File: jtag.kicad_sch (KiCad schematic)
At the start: 1 part, among them J3 PinHeader_2x7_P2mm_SMD_Shroud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

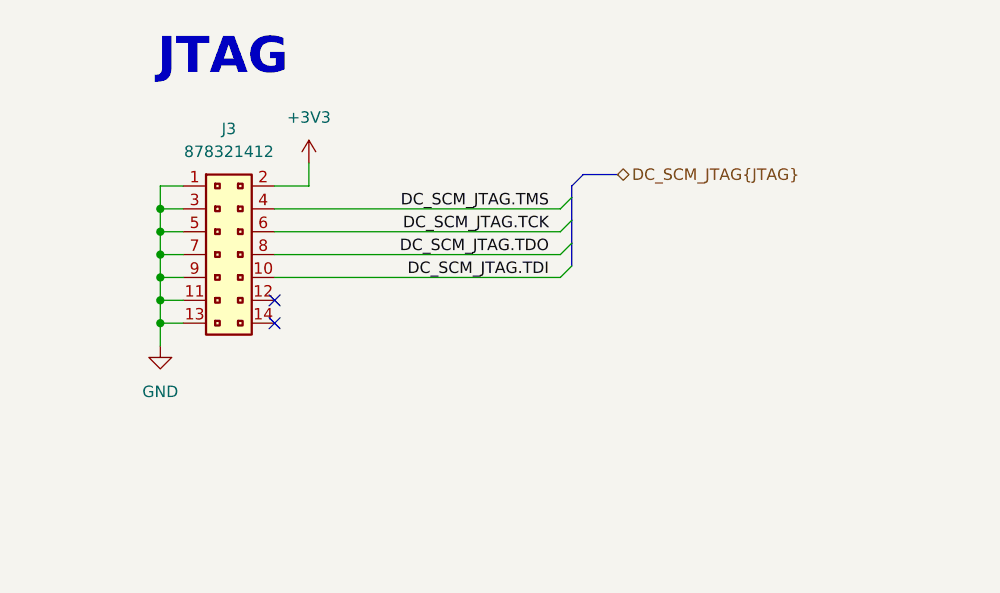
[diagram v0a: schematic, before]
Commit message: [#92504] Clear Wire BUS errors
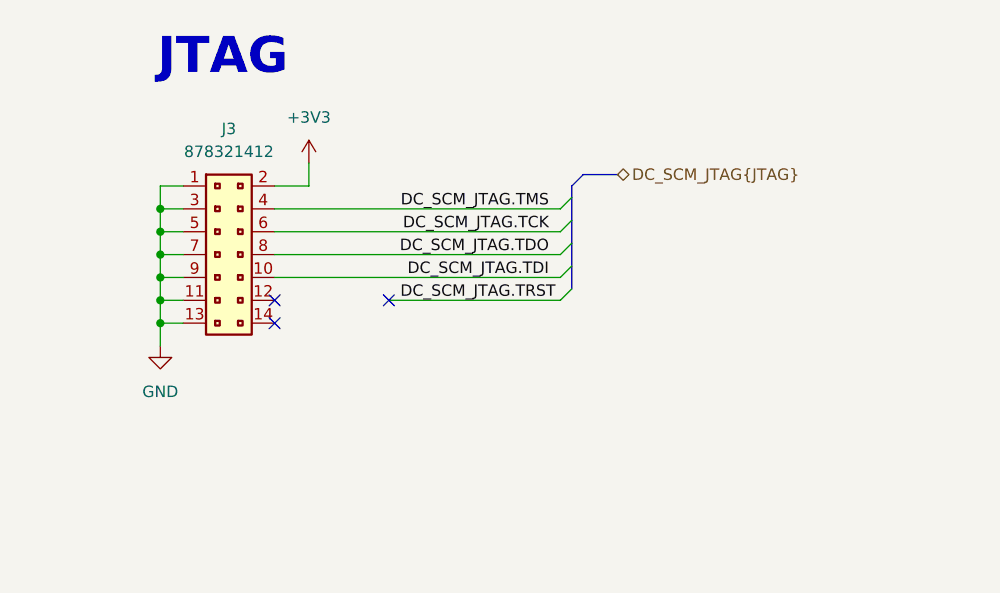
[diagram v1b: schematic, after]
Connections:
- no-connect marks 2 -> 3
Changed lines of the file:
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@@
+	)
+	(no_connect
+		(at 78.74 50.8)
 	)
 	(no_connect
@@
 	)
 	(bus_entry
+		(at 99.06 49.53)
+		(size -1.27 1.27)
+		(stroke
+			(width 0)
+			(type default)
+		)
+	)
+	(bus_entry
 		(at 99.06 41.91)
 		(size -1.27 1.27)
@@
 	(wire
 		(pts
+			(xy 78.74 50.8) (xy 97.79 50.8)
+		)
+		(stroke
+			(width 0)
+			(type default)
+		)
+	)
+	(wire
+		(pts
 			(xy 53.34 50.8) (xy 53.34 53.34)
 		)
@@
 		(pts
 			(xy 53.34 43.18) (xy 53.34 45.72)
+		)
+		(stroke
+			(width 0)
+			(type default)
+		)
+	)
+	(bus
+		(pts
+			(xy 99.06 46.99) (xy 99.06 49.53)
 		)
 		(stroke
@@
 		)
 	)
+	(label "DC_SCM_JTAG.TRST"
+		(at 80.01 50.8 0)
+		(effects
+			(font
+				(size 1.27 1.27)
+			)
+			(justify left bottom)
+		)
+	)

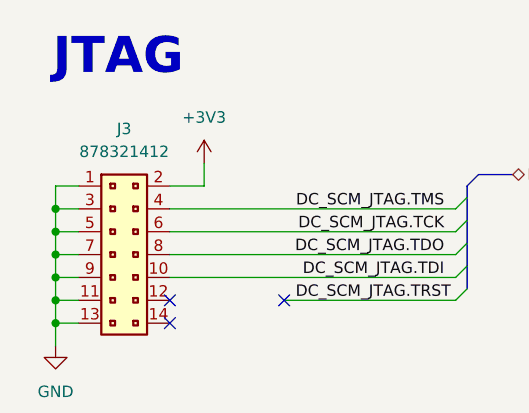
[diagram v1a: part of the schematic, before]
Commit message: [#92504] Update Annotation for connectors
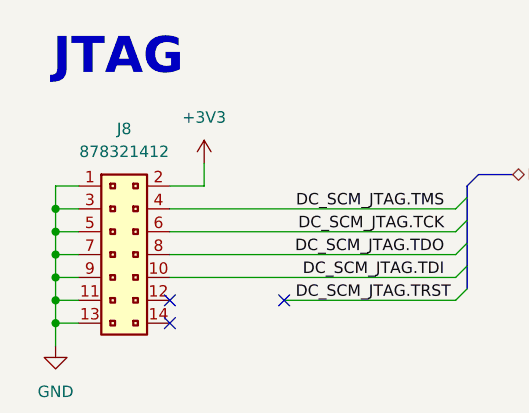
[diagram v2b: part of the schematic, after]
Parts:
- renumbered J3 to J8
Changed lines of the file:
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@@
 		(dnp no)
 		(fields_autoplaced yes)
-		(property "Reference" "J3"
+		(property "Reference" "J8"
 			(at 60.96 31.75 0)
 			(effects
@@
 			(project ""
 				(path "/5d67ef28-5805-4f87-b722-2926dabf7f6e/7d9b23ce-a430-4fe9-932d-039608fe4530"
-					(reference "J3")
+					(reference "J8")
 					(unit 1)
 				)

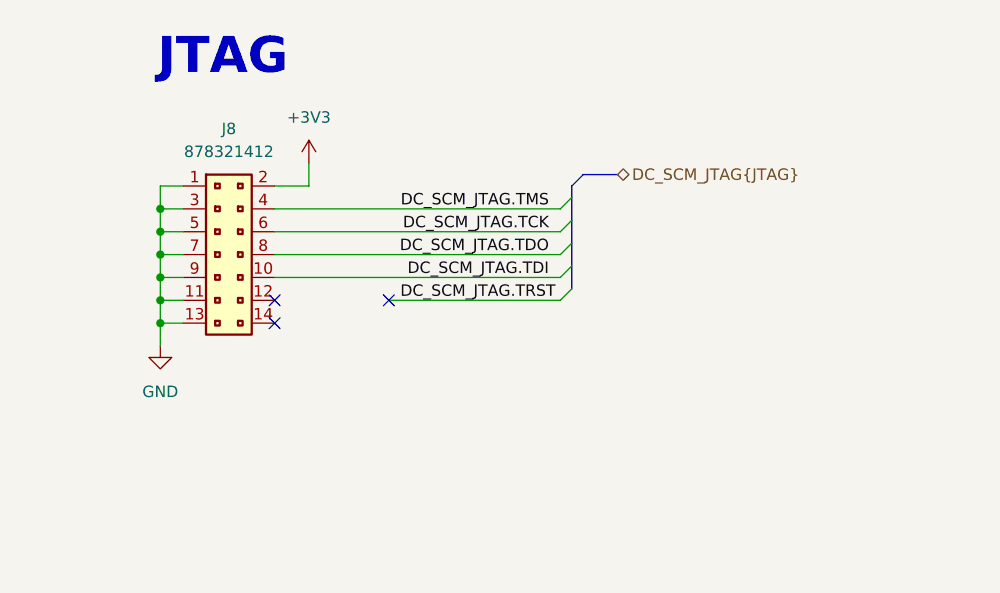
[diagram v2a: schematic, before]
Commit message: [#93090] Change JTAG connector pitch to 1.27
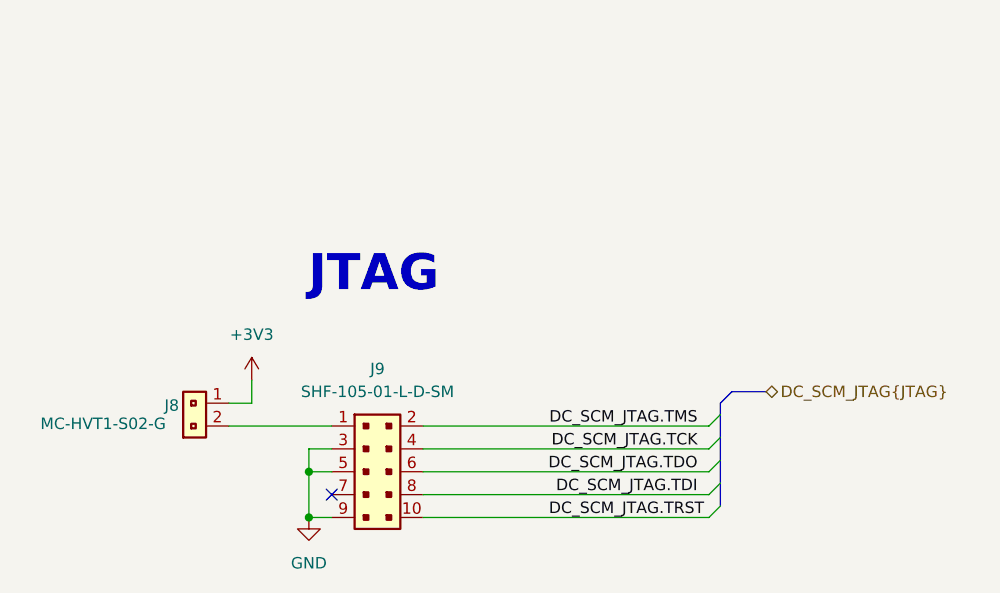
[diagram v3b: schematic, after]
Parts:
- removed J8: PinHeader_2x7_P2mm_SMD_Shrouded_no-locator, antmicro-footprints:PinHeader_2x7_P2mm_SMD_Shrouded_no-locator, symbol antmicroGenericPinHeaders:PinHeader_2x7_P2mm_SMD_Shrouded_no-locator
- added J8: PinHeader_1x2_P1.27mm_Drill0.7mm, antmicro-footprints:PinHeader_1x2_P1.27mm_Drill0.7mm, symbol antmicroGenericPinHeaders:PinHeader_1x2_P1.27mm_Drill0.7mm
- added J9: PinHeader_2x5_P1.27mm_SMD_Shrouded, antmicro-footprints:PinHeader_2x5_P1.27mm_SMD_Shrouded, symbol antmicroGenericPinHeaders:PinHeader_2x5_P1.27mm_SMD_Shrouded
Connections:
- net +3V3: now also J8.1
- net DC_SCM_JTAG.TCK: now also J9.4
- net DC_SCM_JTAG.TDI: now also J9.8
- net DC_SCM_JTAG.TDO: now also J9.6
- net DC_SCM_JTAG.TMS: now also J9.2
- net DC_SCM_JTAG.TRST: now also J9.10
- net GND: now also J9.3, J9.5, J9.9
- new net: J8.2, J9.1
- no-connect marks 3 -> 1
